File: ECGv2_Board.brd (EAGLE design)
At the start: 58.7 x 38 mm, 37 parts, among them IC1 LF347D, IC2 LF347D, IC3 TINY15LS, Q1 BS250

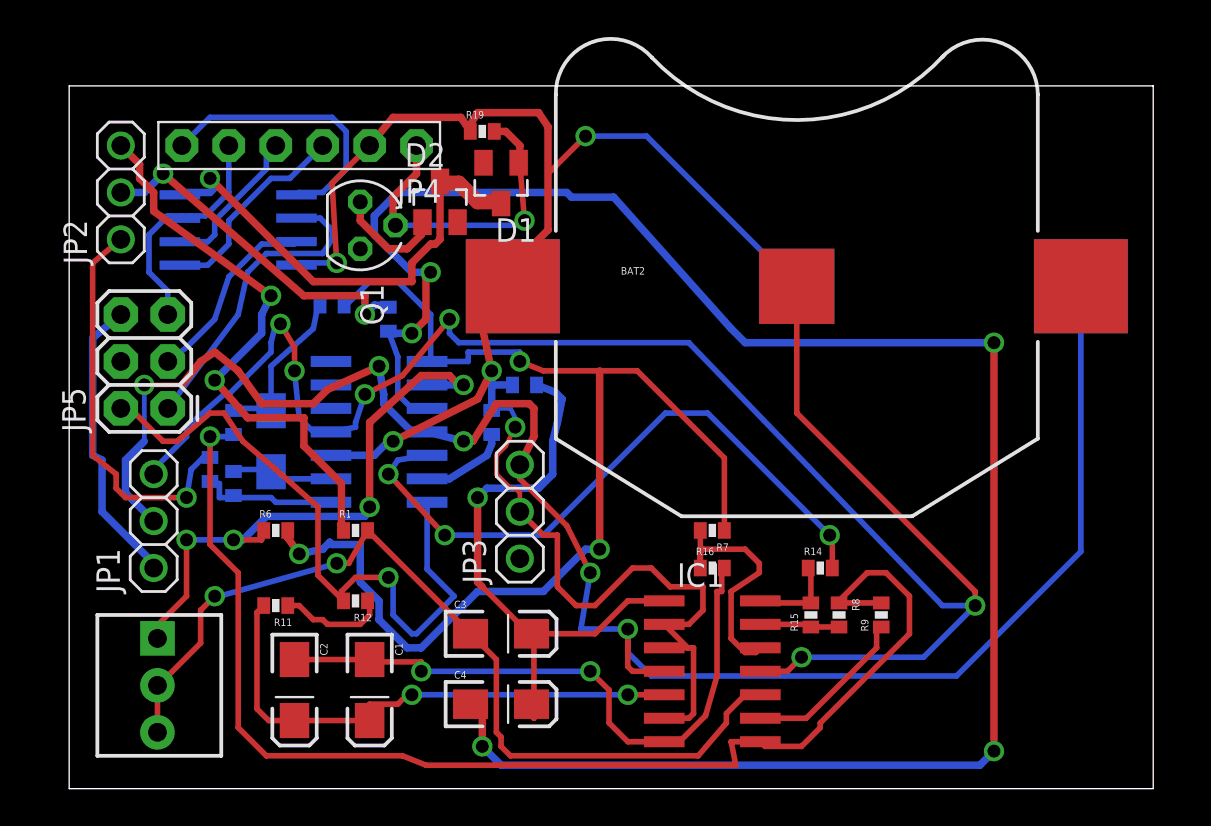
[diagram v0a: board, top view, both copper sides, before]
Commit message: -added missing connection
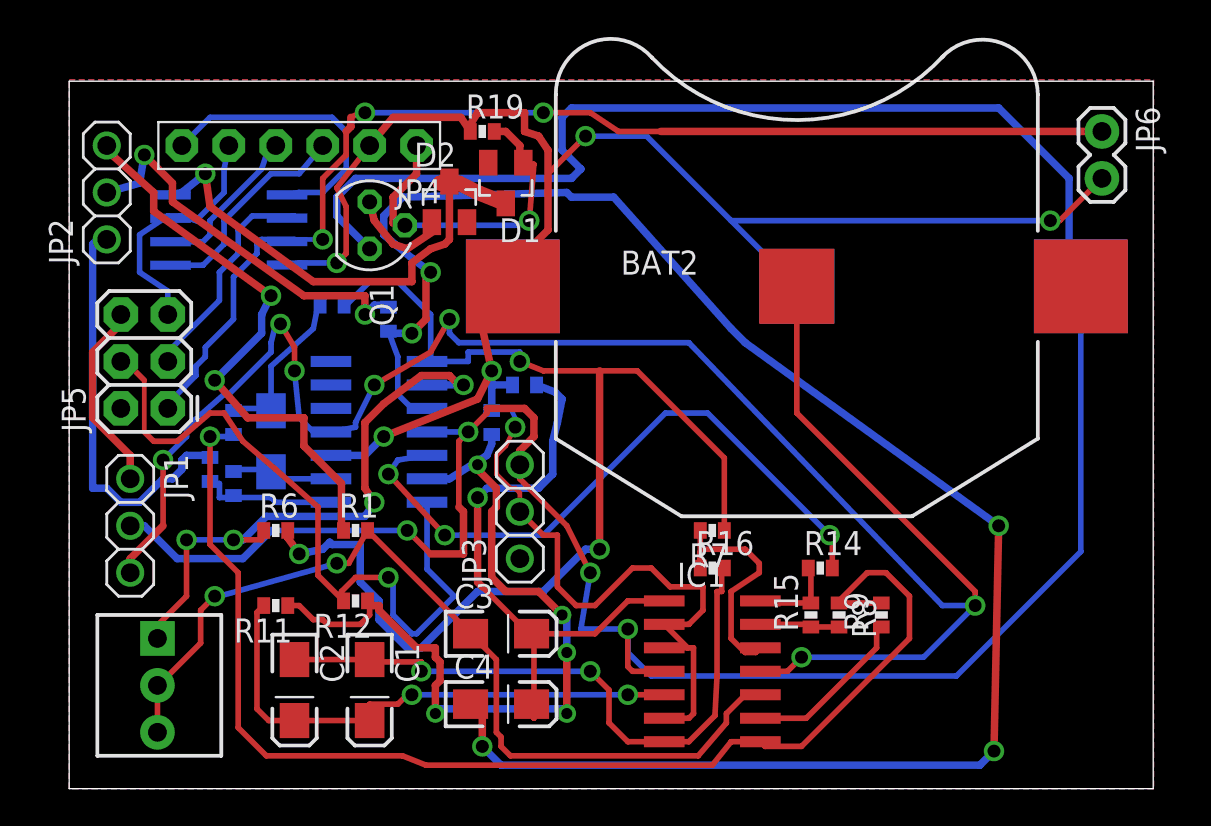
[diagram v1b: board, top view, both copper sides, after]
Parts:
- added JP6: (no value), SparkFun-Connectors:1X02
- moved JP1 1.30 mm to (2.54, 13.2), turned to 270 degrees
- moved JP2 0.76 mm to (1.27, 31.2)
- moved D2 0.51 mm to (19.8, 30.7)
- moved IC3 0.51 mm to (7.87, 29.2)
- moved Q1 0.51 mm to (15.5, 29.5)
- moved D1 0.25 mm to (22.9, 31.8)
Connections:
- removed net 3.3V: Q1.S
- removed net N$27: IC3.2, JP5.1
- removed net N$3: R11.1, R12.1
- new net N$28: IC3.2, JP5.3
- net +3V: now also Q1.S
- net GND: now also JP6.2
- net N$5: now also R11.1, R12.1
- net OUTECG: now also JP5.4; no longer JP5.2
- net OUTPUT: now also JP5.2; no longer JP5.4
- net SEROUT: now also JP5.1, JP6.1; no longer JP5.3
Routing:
- net SEROUT: track 10.3 -> 63.6 mm, vias 0 -> 3
- net +3V: track 99.5 -> 152.7 mm, vias 5 -> 4
- net N$5: track 4.78 -> 43.7 mm, vias 0 -> 5
- net GND: track 107.7 -> 129.0 mm, vias 5 -> 6
- net N$27: track 16.8 -> 0.00 mm
- net N$28: track 0.00 -> 12.5 mm
- net N$18: track 106.5 -> 98.8 mm
- net -3V: track 97.9 -> 103.8 mm, vias 6 -> 7
- net N$3: track 5.84 -> 0.00 mm
- net OUTPPG: track 15.9 -> 10.4 mm
- net OUTECG: track 35.6 -> 38.3 mm
- net N$21: track 18.7 -> 21.2 mm
- net N$26: track 26.0 -> 27.4 mm
- net N$25: track 12.7 -> 13.9 mm
- net N$10: track 68.5 -> 67.6 mm
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- added copper zone on layer 1, net GND
- added copper zone on layer 16, net GND
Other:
- board size 58.7 x 38 mm -> 58.7 x 38.3 mm

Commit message: Major changes
-final commit
-some corrections
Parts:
- Q1: value BS250 -> BSS84; device transistor-small-signal:SOT54E -> transistor-small-signal:SOT23
- moved D1 1.14 mm to (23.9, 32.3), turned to 270 degrees
- moved R8 0.25 mm to (41.1, 8.38)
- moved R9 0.25 mm to (43.4, 8.38)
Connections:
- removed net N$11: IC1.9, R9.1
- new net N$3: IC1.9, R18.2, R18.3, R9.1
- net +3V: now also BAT1.3, Q1.2; no longer Q1.S
- net +5V: now also Q1.1; no longer Q1.G
- net GND: now also BAT2.3, IC1.5; no longer IC1.6
- net N$19: no longer R18.2, R18.3
- net N$2: now also IC1.6; no longer IC1.5
- net N$4: now also Q1.3; no longer Q1.D
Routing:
- net N$3: track 0.00 -> 77.7 mm, vias 0 -> 5
- net +3V: track 152.7 -> 124.7 mm, vias 4 -> 8
- net N$19: track 48.9 -> 34.1 mm
- net N$11: track 9.10 -> 0.00 mm
- net OUTECG: track 38.3 -> 32.1 mm
- net +5V: track 18.5 -> 12.7 mm, vias 1 -> 0
- net N$4: track 6.24 -> 2.34 mm
- net N$9: track 65.6 -> 62.7 mm
- net N$10: track 67.6 -> 70.0 mm
- net N$5: track 43.7 -> 41.6 mm
- net GND: track 129.0 -> 130.7 mm, vias 6 -> 5
- net N$18: track 98.8 -> 97.2 mm
- net N$26: track 27.4 -> 28.7 mm
- net N$20: track 31.1 -> 30.2 mm
- net -3V: track 103.8 -> 104.4 mm
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- removed copper zone on layer 1, net GND
- removed copper zone on layer 16, net GND

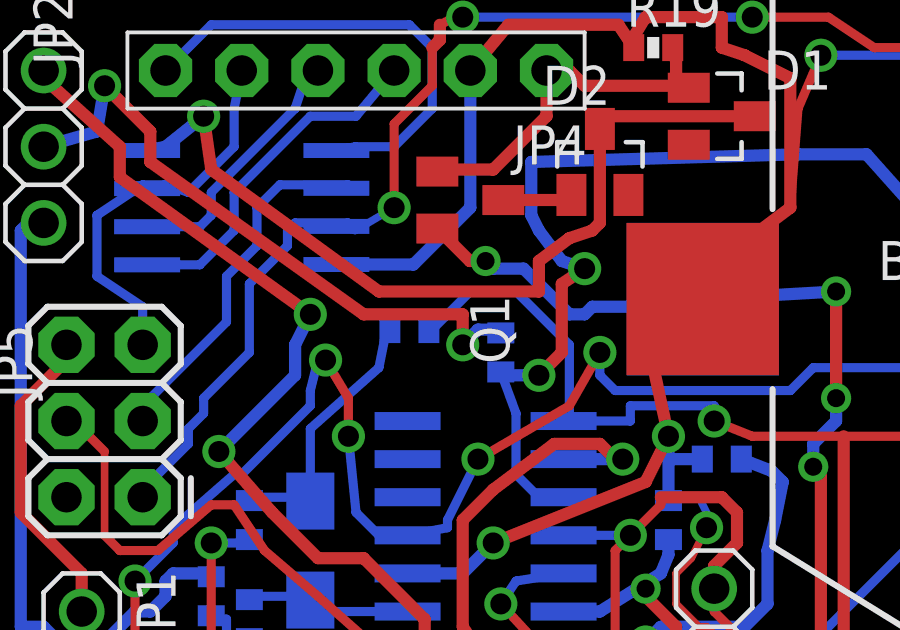
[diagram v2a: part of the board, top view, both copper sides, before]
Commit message: -restructuring
-identification and restructuring of circuit
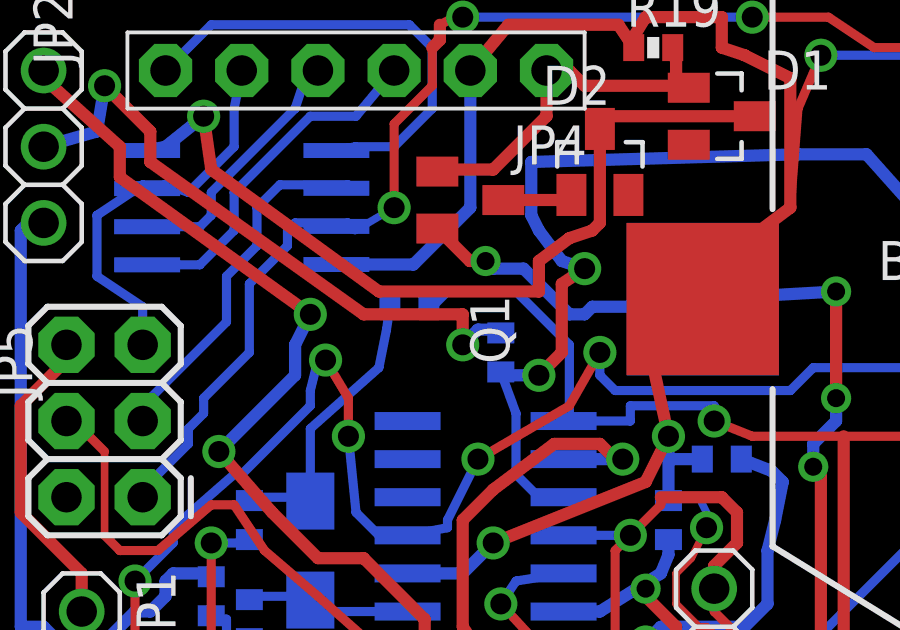
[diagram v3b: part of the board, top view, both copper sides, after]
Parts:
- moved R5 0.76 mm to (13.5, 25.9)
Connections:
- net N$20 renamed (-)
- net N$21 renamed (+)
- net N$22 renamed (REF)
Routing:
- net N$13: track 9.02 -> 9.68 mm
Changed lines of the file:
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@@
 <grid distance="0.01" unitdist="inch" unit="inch" style="lines" multiple="1" display="yes" altdistance="0.025" altunitdist="inch" altunit="inch"/>
 <layers>
-<layer number="1" name="Top" color="4" fill="1" visible="yes" active="yes"/>
+<layer number="1" name="Top" color="4" fill="1" visible="no" active="yes"/>
 <layer number="2" name="Route2" color="1" fill="3" visible="no" active="no"/>
 <layer number="3" name="Route3" color="4" fill="3" visible="no" active="no"/>
@@
 <attribute name="VALUE" x="9.271" y="19.8755" size="0.4064" layer="28" rot="MR270"/>
 </element>
-<element name="R5" library="SparkFun-Passives" package="0402-RES" value="" x="13.462" y="25.146" smashed="yes" rot="MR180">
-<attribute name="NAME" x="12.573" y="24.4475" size="1.3" layer="26" rot="MR180"/>
-<attribute name="VALUE" x="12.3825" y="26.289" size="0.4064" layer="28" rot="MR180"/>
+<element name="R5" library="SparkFun-Passives" package="0402-RES" value="" x="13.462" y="25.908" smashed="yes" rot="MR180">
+<attribute name="NAME" x="12.573" y="25.2095" size="1.3" layer="26" rot="MR180"/>
+<attribute name="VALUE" x="12.3825" y="27.051" size="0.4064" layer="28" rot="MR180"/>
 </element>
 <element name="R6" library="SparkFun-Passives" package="0402-RES" value="" x="10.414" y="12.954" smashed="yes">
@@
 <contactref element="R6" pad="2"/>
 <contactref element="R5" pad="2"/>
-<wire x1="14.112" y1="25.146" x2="14.224" y2="25.146" width="0.3048" layer="16"/>
-<wire x1="14.224" y1="25.146" x2="15.494" y2="26.416" width="0.3048" layer="16"/>
-<wire x1="15.494" y1="26.416" x2="17.018" y2="26.416" width="0.3048" layer="16"/>
+<wire x1="14.112" y1="25.908" x2="14.224" y2="25.908" width="0.3048" layer="16"/>
+<wire x1="14.224" y1="25.908" x2="14.732" y2="26.416" width="0.3048" layer="16"/>
+<wire x1="14.732" y1="26.416" x2="17.018" y2="26.416" width="0.3048" layer="16"/>
 <wire x1="17.018" y1="26.416" x2="18.796" y2="24.638" width="0.3048" layer="16"/>
 <wire x1="18.796" y1="24.638" x2="18.796" y2="22.292" width="0.3048" layer="16"/>
@@
 <wire x1="10.16" y1="19.558" x2="10.16" y2="19.43" width="0.3048" layer="16"/>
 <wire x1="12.7" y1="25.146" x2="12.446" y2="23.876" width="0.3048" layer="16"/>
-<wire x1="12.7" y1="25.146" x2="12.812" y2="25.146" width="0.3048" layer="16"/>
+<wire x1="12.7" y1="25.146" x2="12.812" y2="25.908" width="0.3048" layer="16"/>
 </signal>
 <signal name="N$14">
@@
 <contactref element="JP3" pad="1"/>
 </signal>
-<signal name="N$20">
+<signal name="(-)">
 <contactref element="R1" pad="1"/>
 <contactref element="JP2" pad="3"/>
@@
 <wire x1="10.414" y1="17.526" x2="11.938" y2="17.526" width="0.4064" layer="1"/>
 </signal>
-<signal name="N$21">
+<signal name="(+)">
 <contactref element="JP2" pad="2"/>
 <contactref element="R2" pad="1"/>
@@
 <via x="15.24" y="24.638" extent="1-16" drill="0.7" diameter="0.8128"/>
 </signal>
-<signal name="N$22">
+<signal name="(REF)">
 <contactref element="R3" pad="1"/>
 <contactref element="JP2" pad="1"/>
